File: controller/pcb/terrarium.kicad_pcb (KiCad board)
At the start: 4 copper layers, 90 x 90 mm, 78 parts, among them K1 G3MB-202P, K2 G3MB-202P, K3 G3MB-202P, P1 USB_C_Plug_USB2.0, Q1 S8050, Q2 S8050, Q3 S8050, Q4 S8050, Q5 BC817, Q6 BC817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

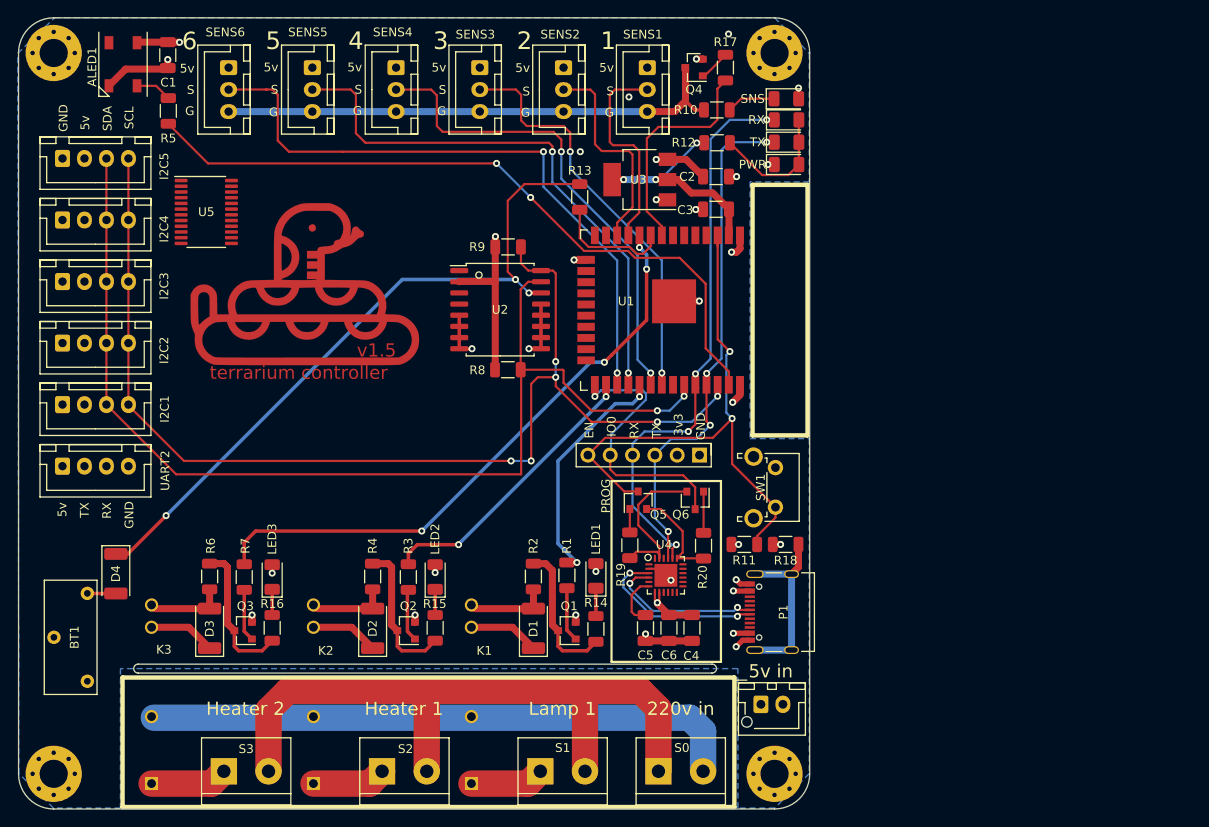
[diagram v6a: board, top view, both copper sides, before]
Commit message: add multiplexer for i2c, rearrange everything
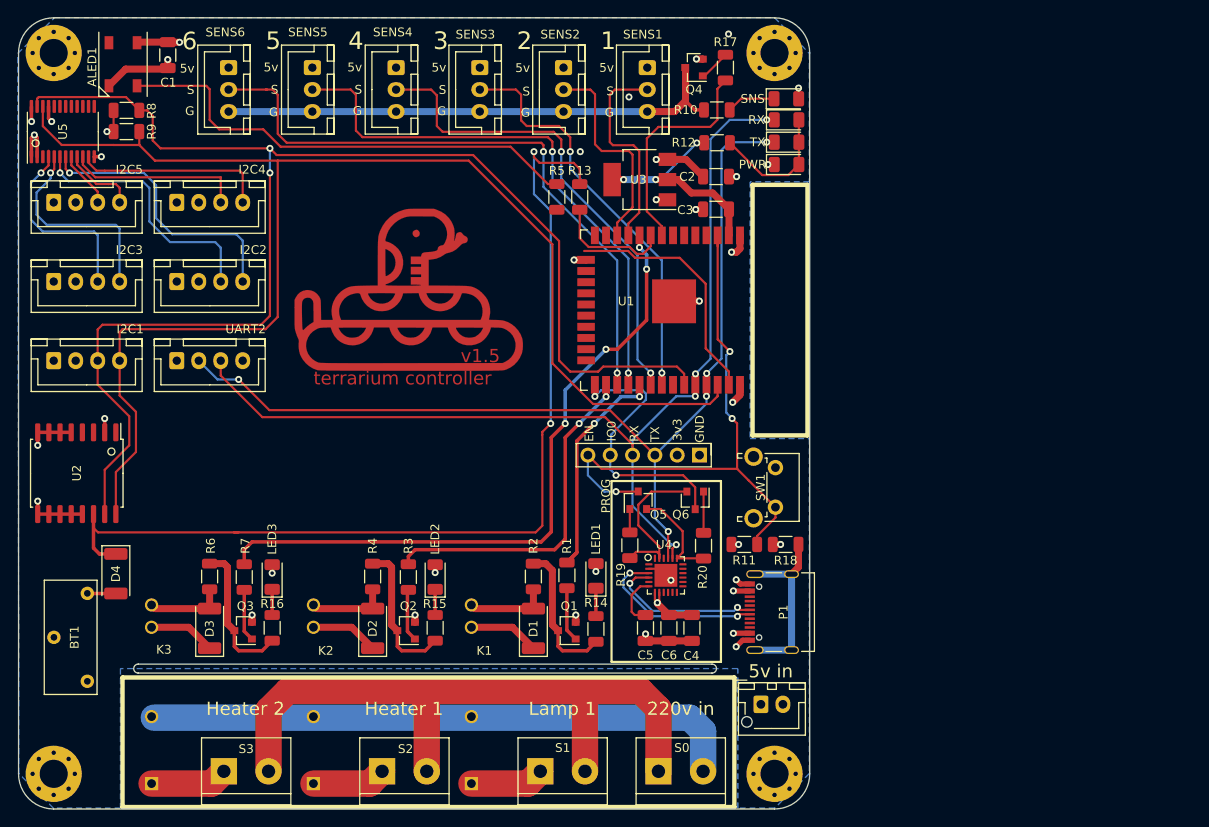
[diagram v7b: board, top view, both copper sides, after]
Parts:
- moved R8 52.5 mm to (53.3, 33.5)
- moved U2 51.6 mm to (47.6, 74.8), turned to 270 degrees
- moved R9 45.4 mm to (53.3, 35.9)
- moved R5 45.3 mm to (102.2, 43.4)
- moved U5 18.7 mm to (46.0, 35.9), turned to 90 degrees
- moved UART2 17.7 mm to (59.0, 62.0)
- moved I2C2 14.8 mm to (59.0, 53.0)
- moved I2C4 13.2 mm to (59.0, 44.0)
- moved G*** 11.8 mm to (85.4, 53.9)
- moved I2C1 5.10 mm to (45.0, 62.0)
- moved I2C5 5.10 mm to (45.0, 44.0)
- moved I2C3 1.00 mm to (45.0, 53.0)
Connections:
- I2C2 pad 3: SDA -> SDA_2
- I2C2 pad 4: SCL -> SCL_2
- I2C3 pad 3: SDA -> SDA_1
- I2C3 pad 4: SCL -> SCL_1
- I2C4 pad 3: SDA -> SDA_0
- I2C4 pad 4: SCL -> SCL_0
- I2C5 pad 3: SDA -> SDA_3
- I2C5 pad 4: SCL -> SCL_3
- U5 pad 10: Net-(U5-Pad10) -> SDA_0
- U5 pad 11: Net-(U5-Pad11) -> SCL_0
- U5 pad 4: Net-(U5-Pad4) -> SDA_1
- U5 pad 5: Net-(U5-Pad5) -> SCL_1
- U5 pad 6: Net-(U5-Pad6) -> SDA_2
- U5 pad 7: Net-(U5-Pad7) -> SCL_2
- U5 pad 8: Net-(U5-Pad8) -> SDA_3
- U5 pad 9: Net-(U5-Pad9) -> SCL_3
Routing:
- net TX: track 59.1 -> 112.9 mm, vias 4 -> 5
- net G23: track 81.2 -> 28.0 mm, vias 2 -> 0
- net RX: track 65.5 -> 116.4 mm
- net Net-(ALED1-Pad4): track 4.45 -> 54.7 mm
- net SDA: track 125.5 -> 162.1 mm
- net SCL: track 130.1 -> 162.1 mm, vias 6 -> 0
- net Net-(D4-Pad1): track 80.2 -> 112.2 mm, vias 3 -> 2
- net SCL_2: track 0.00 -> 31.8 mm, vias 0 -> 1
- net SDA_2: track 0.00 -> 29.7 mm, vias 0 -> 1
- net SCL_1: track 0.00 -> 23.6 mm, vias 0 -> 1
- net SDA_1: track 0.00 -> 22.3 mm, vias 0 -> 1
- net SCL_0: track 0.00 -> 22.0 mm
- net SDA_0: track 0.00 -> 20.1 mm
- net +3V3: track 45.3 -> 32.5 mm, vias 5 -> 7
- net SCL_3: track 0.00 -> 8.49 mm
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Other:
- board text added: "terrarium controller v1.5 github.com/brushknight/terrarium github.com/brushknight/terrarium-hardware"
- board text removed: "terrarium controller v1.4 github.com/brushknight/terrarium github.com/brushknight/terrarium-hardware"

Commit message: fix CP2102, minor bugs
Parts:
- U4: value CP2102N-A01-GQFN24 -> CP2102N-A02-GQFN24; footprint Package_DFN_QFN:QFN-24-1EP_4x4mm_P0.5mm_EP2.6x2.6mm -> cp2102:Silicon_Labs-CP2102N-A02-GQFN24-IPC_A
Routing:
- net G23: track 28.0 -> 33.9 mm
- net Net-(Q6-Pad2): track 17.4 -> 18.2 mm
- net GND: track 59.4 -> 60.1 mm, vias 26 -> 23
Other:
- net class IC added: clearance 0.1, trace_width 0.25, via_dia 0.8, via_drill 0.4
